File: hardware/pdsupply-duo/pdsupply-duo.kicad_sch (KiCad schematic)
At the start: 3 parts

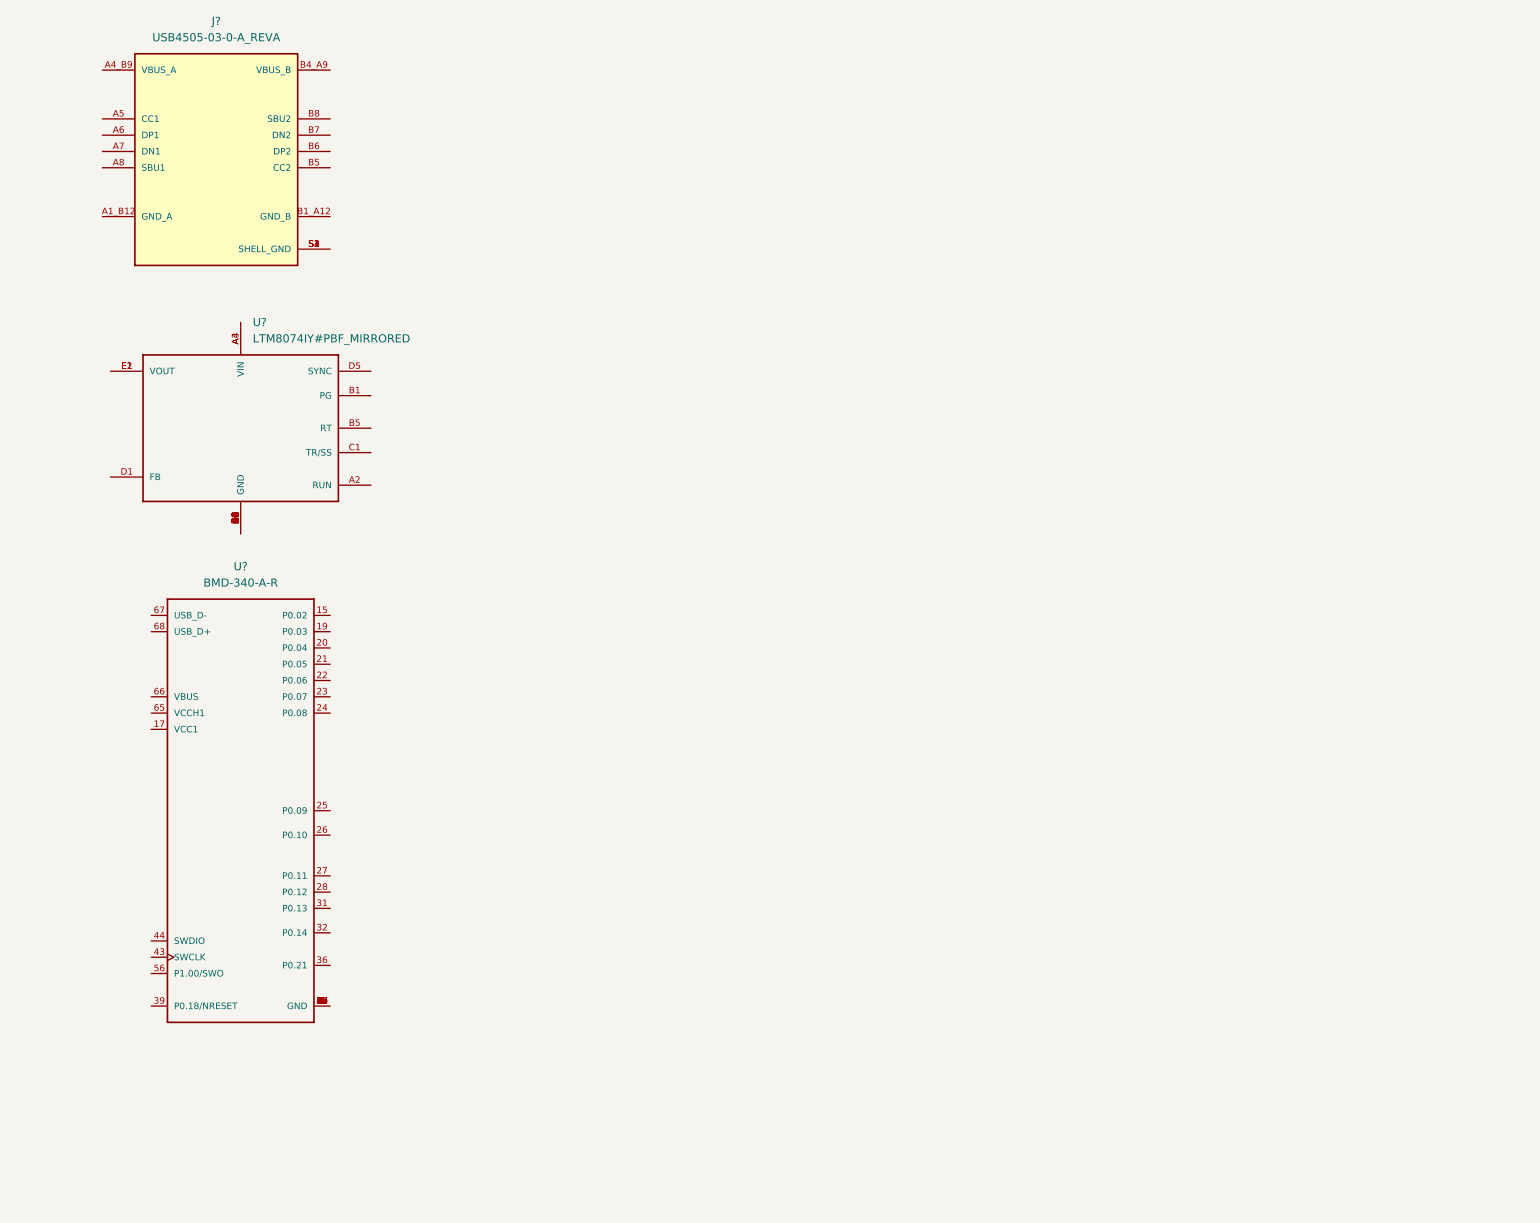
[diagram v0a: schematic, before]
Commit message: Added few more parts to comp folder
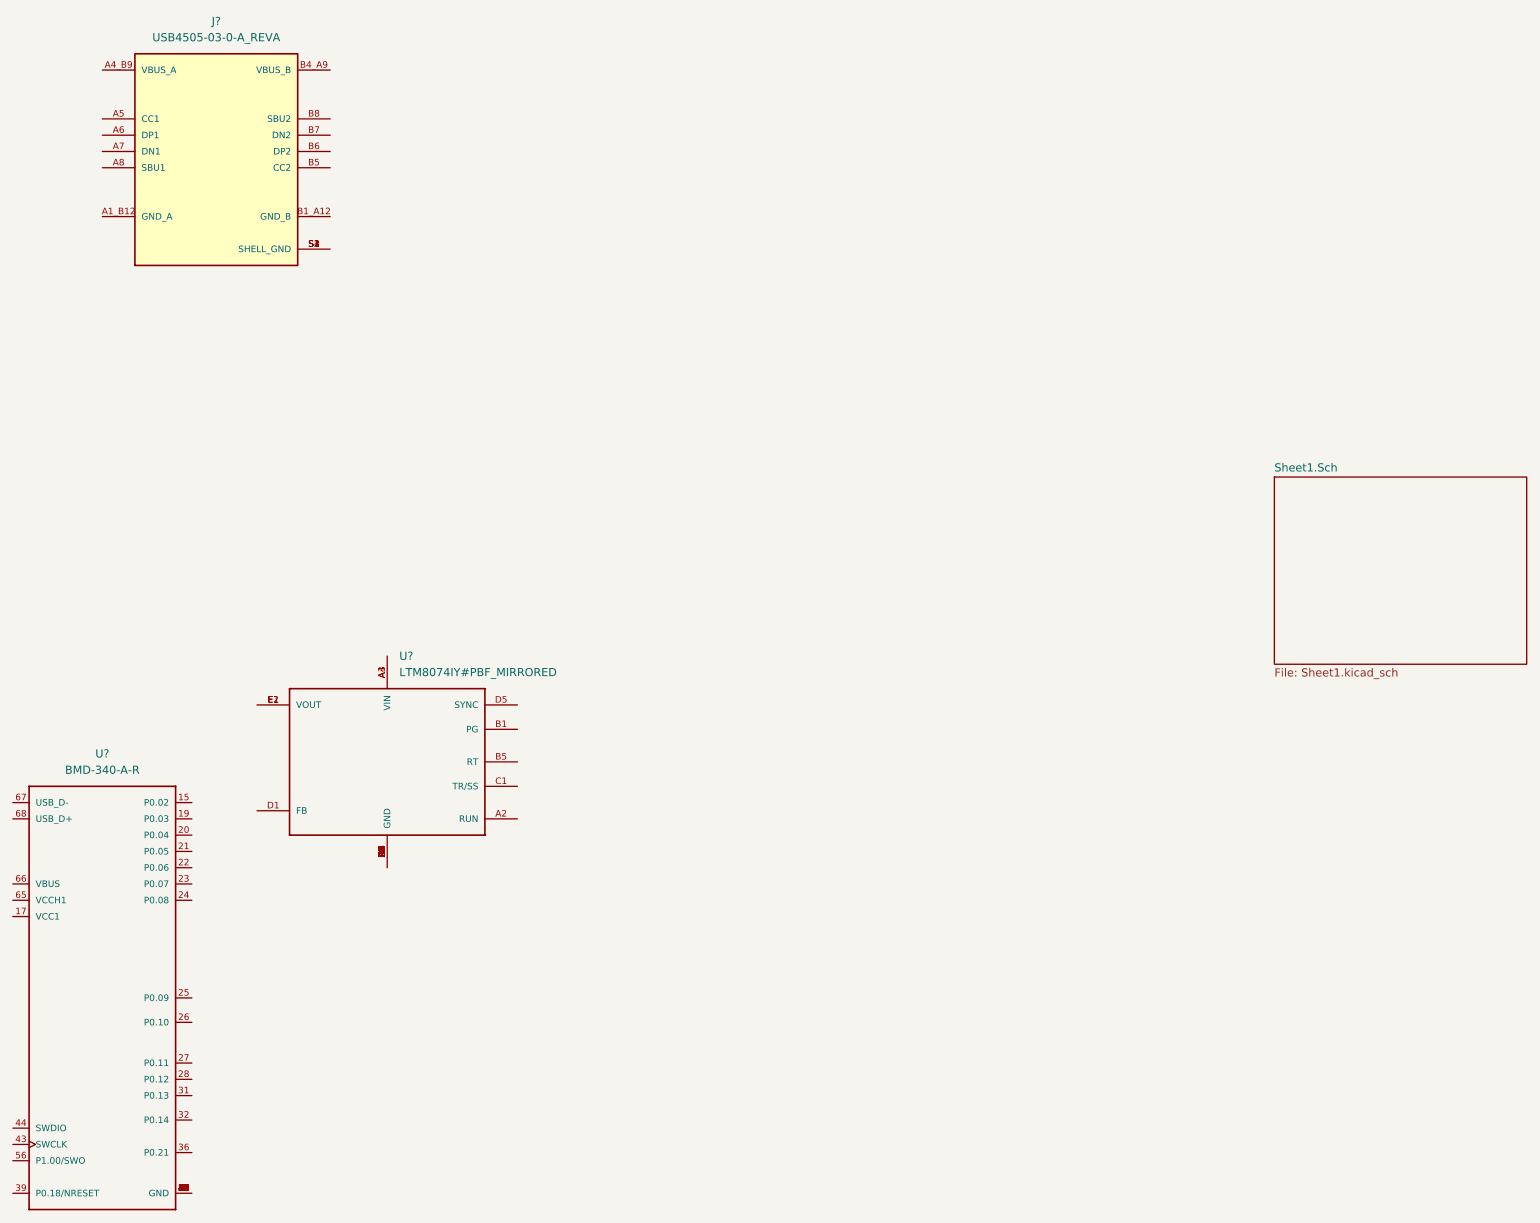
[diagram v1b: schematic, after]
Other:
- added sheet Sheet1.Sch (Sheet1.kicad_sch)
- moved on the sheet: U?
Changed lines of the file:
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@@
     (rev "1")
   )
-  (symbol (lib_id "LTM8074IY_PBF:LTM8074IY#PBF_MIRRORED") (at 67.31 95.25 0) (unit 1)
+  (symbol (lib_id "LTM8074IY_PBF:LTM8074IY#PBF_MIRRORED") (at 90.17 147.32 0) (unit 1)
     (in_bom yes) (on_board yes) (fields_autoplaced)
-    (property "Reference" "U?" (id 0) (at 69.1897 77.47 0)
+    (property "Reference" "U?" (id 0) (at 92.0497 129.54 0)
       (effects (font (size 1.27 1.27)) (justify left))
     )
-    (property "Value" "LTM8074IY#PBF_MIRRORED" (id 1) (at 69.1897 80.01 0)
+    (property "Value" "LTM8074IY#PBF_MIRRORED" (id 1) (at 92.0497 132.08 0)
       (effects (font (size 1.27 1.27)) (justify left))
     )
-    (property "Footprint" "BGA25C65P5X5_400X400X198N" (id 2) (at 67.31 91.44 0)
+    (property "Footprint" "BGA25C65P5X5_400X400X198N" (id 2) (at 90.17 143.51 0)
       (effects (font (size 1.27 1.27)) (justify left bottom) hide)
     )
-    (property "Datasheet" "A" (id 3) (at 67.31 95.25 0)
+    (property "Datasheet" "A" (id 3) (at 90.17 147.32 0)
       (effects (font (size 1.27 1.27)) (justify left bottom) hide)
     )
-    (property "Field4" "IPC 7351B" (id 4) (at 67.31 95.25 0)
+    (property "Field4" "IPC 7351B" (id 4) (at 90.17 147.32 0)
       (effects (font (size 1.27 1.27)) (justify left bottom) hide)
     )
-    (property "Field5" "1.98 mm" (id 5) (at 67.31 95.25 0)
+    (property "Field5" "1.98 mm" (id 5) (at 90.17 147.32 0)
       (effects (font (size 1.27 1.27)) (justify left bottom) hide)
     )
-    (property "Field6" "Analog Devices" (id 6) (at 67.31 91.44 0)
+    (property "Field6" "Analog Devices" (id 6) (at 90.17 143.51 0)
       (effects (font (size 1.27 1.27)) (justify left bottom) hide)
     )
@@
     (pin "E5")
   )
-  (symbol (lib_id "BMD-340-A-R:BMD-340-A-R") (at 66.04 163.83 0) (unit 1)
+  (symbol (lib_id "BMD-340-A-R:BMD-340-A-R") (at 44.45 193.04 0) (unit 1)
     (in_bom yes) (on_board yes) (fields_autoplaced)
-    (property "Reference" "U?" (id 0) (at 67.31 115.57 0))
-    (property "Value" "BMD-340-A-R" (id 1) (at 67.31 118.11 0))
-    (property "Footprint" "RIGADO_BMD-340-A-R" (id 2) (at 54.61 191.77 0)
+    (property "Reference" "U?" (id 0) (at 45.72 144.78 0))
+    (property "Value" "BMD-340-A-R" (id 1) (at 45.72 147.32 0))
+    (property "Footprint" "RIGADO_BMD-340-A-R" (id 2) (at 33.02 220.98 0)
       (effects (font (size 1.27 1.27)) (justify left bottom) hide)
     )
-    (property "Datasheet" "Rigado" (id 3) (at 66.04 163.83 0)
+    (property "Datasheet" "Rigado" (id 3) (at 44.45 193.04 0)
       (effects (font (size 1.27 1.27)) (justify left bottom) hide)
     )
-    (property "Field4" "None" (id 4) (at 66.04 163.83 0)
+    (property "Field4" "None" (id 4) (at 44.45 193.04 0)
       (effects (font (size 1.27 1.27)) (justify left bottom) hide)
     )
-    (property "Field5" "Unavailable" (id 5) (at 66.04 163.83 0)
+    (property "Field5" "Unavailable" (id 5) (at 44.45 193.04 0)
       (effects (font (size 1.27 1.27)) (justify left bottom) hide)
     )
-    (property "Field6" "Bluetooth Low Energy 5.0 Module" (id 6) (at 54.61 191.77 0)
+    (property "Field6" "Bluetooth Low Energy 5.0 Module" (id 6) (at 33.02 220.98 0)
       (effects (font (size 1.27 1.27)) (justify left bottom) hide)
     )
-    (property "Field7" "BMD-340-A-R" (id 7) (at 54.61 191.77 0)
+    (property "Field7" "BMD-340-A-R" (id 7) (at 33.02 220.98 0)
       (effects (font (size 1.27 1.27)) (justify left bottom) hide)
     )
-    (property "Field8" "10.66 USD" (id 8) (at 66.04 163.83 0)
+    (property "Field8" "10.66 USD" (id 8) (at 44.45 193.04 0)
       (effects (font (size 1.27 1.27)) (justify left bottom) hide)
     )
@@
     (pin "S4")
   )
+  (sheet (at 228.6 101.6) (size 39.37 29.21) (fields_autoplaced)
+    (stroke (width 0.1524) (type solid) (color 0 0 0 0))
+    (fill (color 0 0 0 0.0000))
+    (property "Sheet name" "Sheet1.Sch" (id 0) (at 228.6 100.8884 0)
+      (effects (font (size 1.27 1.27)) (justify left bottom))
+    )
+    (property "Sheet file" "Sheet1.kicad_sch" (id 1) (at 228.6 131.3946 0)
+      (effects (font (size 1.27 1.27)) (justify left top))
+    )
+  )
   (sheet_instances
     (path "/" (page "1"))
+    (path "/5b3bdcf4-2f94-450c-9715-c0affb71f163" (page "2"))
   )
   (symbol_instances
@@
       (reference "J?") (unit 1) (value "USB4505-03-0-A_REVA") (footprint "GCT_USB4505-03-0-A_REVA")
     )
+    (path "/5b3bdcf4-2f94-450c-9715-c0affb71f163/63577af0-0735-4477-8485-c79396b3213d"
+      (reference "U?") (unit 1) (value "MCP4017-xxxxLT") (footprint "Package_TO_SOT_SMD:SOT-363_SC-70-6")
+    )
     (path "/6b29acfa-bec5-4c4a-9b31-80c598169c2e"
       (reference "U?") (unit 1) (value "LTM8074IY#PBF_MIRRORED") (footprint "BGA25C65P5X5_400X400X198N")
+    )
+    (path "/5b3bdcf4-2f94-450c-9715-c0affb71f163/8320cf76-9c31-4423-a485-22baae73e299"
+      (reference "U?") (unit 1) (value "LTM8026IV#PBF") (footprint "LGA81C127P8X11_1125X1500X292N")
     )
     (path "/cbcbd910-1942-4f08-852a-8ef0c7e065dc"
       (reference "U?") (unit 1) (value "BMD-340-A-R") (footprint "RIGADO_BMD-340-A-R")
     )
+    (path "/5b3bdcf4-2f94-450c-9715-c0affb71f163/eb805e0e-cf1b-421b-bcc2-90a4d1a36ae9"
+      (reference "U?") (unit 1) (value "ACS71240KEXBLT-050U5") (footprint "XDCR_ACS71240KEXBLT-050U5")
+    )
   )
